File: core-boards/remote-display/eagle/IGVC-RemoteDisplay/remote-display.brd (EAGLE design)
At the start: 92 x 52.5 mm, 32 parts, among them IC1 ATMEGA8, J1 B2PS-VH(LF)(SN), SW1 SPST_TACT-EVQQ2, T1 R-78E5.0-1.0, U1 ST7920, U2 MIC550X, X1 16MHz

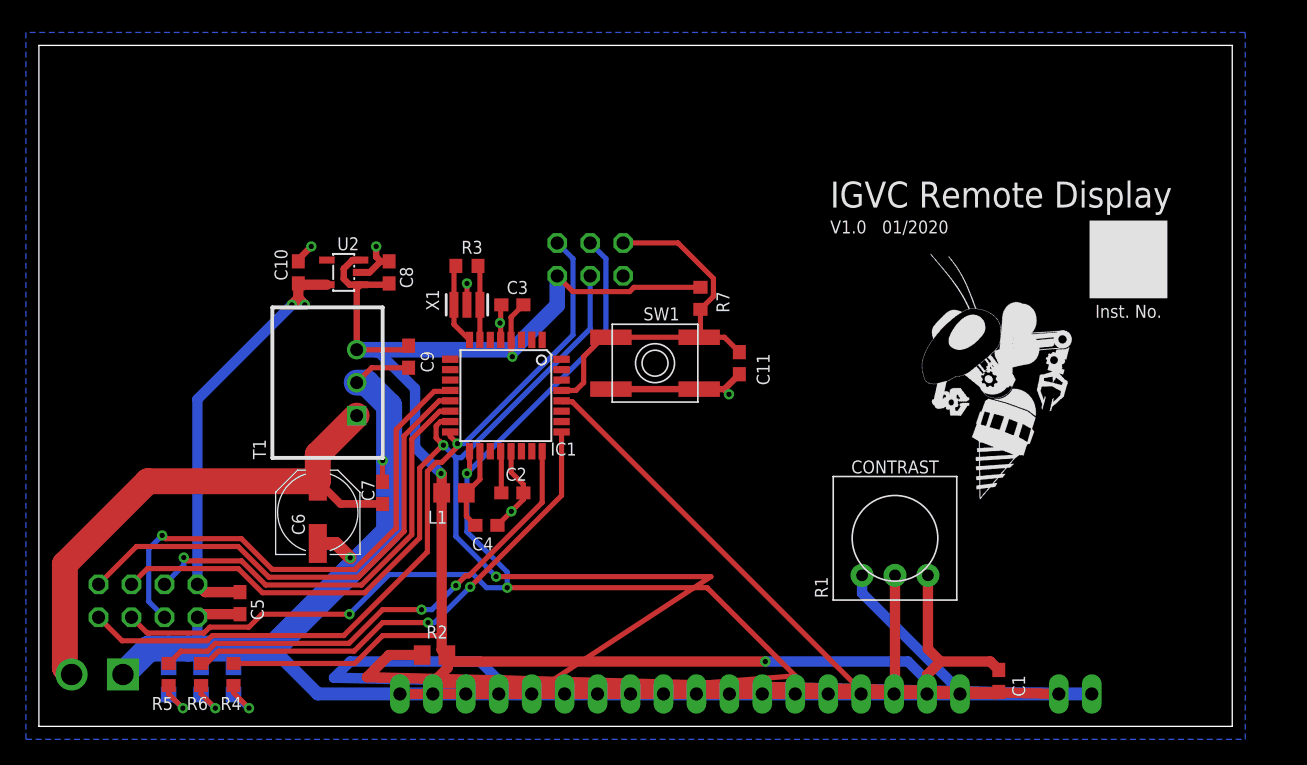
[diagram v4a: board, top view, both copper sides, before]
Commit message: Reroute Remote Display Panel
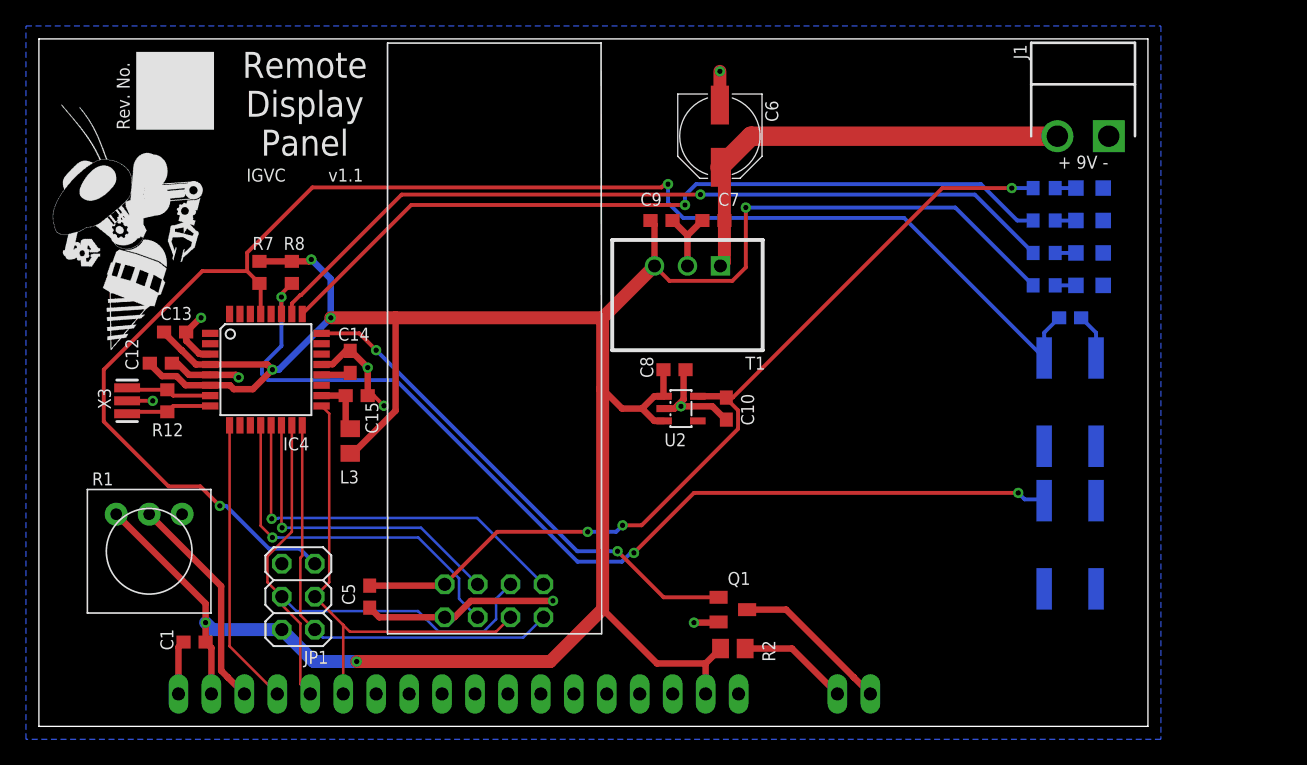
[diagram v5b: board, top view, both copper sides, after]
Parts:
- removed C2, C3, C4: 0.1uF, resistor:C0603
- removed IC1: ATMEGA8, atmel:TQFP32-08
- removed L1: 10uH, IGVC-Remote:0805
- removed U$1: ROBOBUZZ1.0X, RoboJackets-Aesthetics:ROBOBUZZ_1.0X
- removed X1: 16MHz, IGVC-Remote:RESONATOR
- added 3V3_ON: GREEN, led:CHIP-LED0805
- added C12, C13, C14, C15: 0.1uF, resistor:C0603
- added IC4: MEGA8-AI, atmel:TQFP32-08
- added L3: 10uH, IGVC-Remote:0805
- added Q1: (no value), adafruit:SOT23
- added R12: 1M, resistor:R0603
- added R8: 10K, resistor:R0603
- added SW2: SPST_TACT-EVQQ2, adafruit:EVQ-Q2
- added U$2: ROBOBUZZ1.0X, RoboJackets-Aesthetics:ROBOBUZZ_1.0X
- added X3: 16MHz, IGVC-Remote:RESONATOR
- R3: value 1M -> 220R
- moved J1 86.6 mm to (80.5, 45.5), flipped to the top, turned to 180 degrees
- moved D1 79.4 mm to (81.0, 39.0), turned to 90 degrees
- moved R5 76.0 mm to (77.5, 39.0), flipped to the bottom, turned to 180 degrees
- moved D2 76.0 mm to (81.0, 36.5), turned to 90 degrees
- moved ON 72.7 mm to (81.0, 34.0), turned to 90 degrees
- moved R6 72.7 mm to (77.5, 36.5), flipped to the bottom, turned to 180 degrees
- moved R4 69.3 mm to (77.5, 34.0), flipped to the bottom, turned to 180 degrees
- moved C1 62.1 mm to (12.0, 6.50), turned to 180 degrees
- moved R1 57.5 mm to (8.50, 13.5), turned to 180 degrees
- moved R3 44.9 mm to (77.5, 41.5), flipped to the bottom
- moved C6 42.4 mm to (52.5, 45.5), turned to 270 degrees
- moved C10 34.6 mm to (53.0, 24.5), turned to 270 degrees
- moved JP1 34.4 mm to (20.0, 10.0), flipped to the top, turned to 90 degrees
- moved R7 34.1 mm to (17.0, 35.0)
- moved C7 33.0 mm to (52.0, 39.0), turned to 180 degrees
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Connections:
- net N$3 renamed LCD_BL
- removed net STAT1: IC1.24, R5.1
- removed net STAT2: IC1.25, R6.1
- new net BL_DRAIN: Q1.3, U1.20
- new net BL_GATE: IC4.24, Q1.1
- new net BL_SW: IC4.27, R8.1, SW2.B
- new net DEBUG1: IC4.25, R5.1
- new net DEBUG2: IC4.26, R6.1
- new net PWR_LED1: 3V3_ON.A, R3.2
- net !RESET: now also IC4.29; no longer IC1.29, SW1.B'
- net +3V3: now also R3.1
- net +5V: now also C12.1, C13.1, IC4.4, IC4.6, L3.2, R8.2; no longer C3.1, IC1.4, L1.2
- net AREF: now also C14.1, IC4.20; no longer C2.1, IC1.20
- net AVCC: now also C15.1, IC4.18, L3.1; no longer C4.1, IC1.18, L1.1
- net GDO0: now also IC4.12; no longer IC1.12
- net GDO2: now also IC4.13; no longer IC1.13
- net GND: now also 3V3_ON.C, C12.2, C13.2, C14.2, C15.2, IC4.21, IC4.3, IC4.5, Q1.2, SW2.A, SW2.A', X3.2; no longer C2.2, C3.2, C4.2, IC1.21, IC1.5, U1.20, X1.2
- net LCD_CS: now also IC4.9; no longer IC1.28
- net MISO: now also IC4.16; no longer IC1.16
- net MOSI: now also IC4.15; no longer IC1.15
- net RF_CS: now also IC4.14; no longer IC1.14
- net SCK: now also IC4.17; no longer IC1.17
- net XTAL1: now also IC4.7, R12.2, X3.1; no longer IC1.7, R3.1, X1.3
- net XTAL2: now also IC4.8, R12.1, X3.3; no longer IC1.8, R3.2, X1.1
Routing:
- net GND: track 353.4 -> 61.6 mm, vias 8 -> 9
- net !RESET: track 30.1 -> 117.8 mm, vias 0 -> 2
- net BL_SW: track 0.00 -> 78.0 mm, vias 0 -> 3
- net SCK: track 109.2 -> 37.4 mm, vias 3 -> 0
- net DEBUG2: track 0.00 -> 63.3 mm, vias 0 -> 1
- net DEBUG1: track 0.00 -> 62.1 mm, vias 0 -> 1
- net MOSI: track 99.6 -> 44.0 mm, vias 2 -> 0
- net LCD_BL: track 58.3 -> 8.56 mm
- net BL_GATE: track 0.00 -> 39.0 mm, vias 0 -> 2
- net LCD_CS: track 60.3 -> 22.2 mm
- net STAT2: track 38.1 -> 0.00 mm, vias 2 -> 0
- net STAT1: track 37.9 -> 0.00 mm, vias 2 -> 0
- net +3V3: track 33.9 -> 68.9 mm, vias 2 -> 3
- net CONTRAST: track 42.2 -> 16.9 mm
- net MISO: track 59.6 -> 34.8 mm, vias 1 -> 0
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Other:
- board size 92 x 52.5 mm -> 85.5 x 53 mm
- board text added: "+ 9V -"
- board text added: "3.3V"
- board text added: "5V"
- board text added: "D1"
- board text added: "D2"
- board text added: "IGVC"
- board text added: "Remote Display Panel"
- board text added: "Rev. No."
- board text added: "v1.1"
- board text removed: "- 9V +"
- board text removed: "01/2020"
- board text removed: "CONTRAST"
- board text removed: "IGVC Remote Display"
- board text removed: "Inst. No."
- board text removed: "V1.0"

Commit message: Extraneous changes to remote display
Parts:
- added C2: 10uF, resistor:C0805
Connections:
- net +5V: now also C2.1
- net GND: now also C2.2
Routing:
- net GND: track 61.6 -> 63.5 mm, vias 9 -> 10
- net +5V: track 211.8 -> 212.8 mm
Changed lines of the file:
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@@
 <attribute name="VALUE" x="50.325" y="10.905" size="1.27" layer="27" rot="R270"/>
+</element>
+<element name="C2" library="resistor" library_urn="urn:adsk.eagle:library:348" package="C0805" package3d_urn="urn:adsk.eagle:package:23617/2" value="10uF" x="25" y="33.5" smashed="yes" rot="R90">
+<attribute name="NAME" x="23.365" y="32.865" size="1" layer="25" rot="R90"/>
+<attribute name="VALUE" x="26.905" y="32.865" size="1.27" layer="27" rot="R90"/>
 </element>
 </elements>
@@
 <wire x1="52.5" y1="47.9" x2="52.5" y2="50.5" width="1" layer="1"/>
 <via x="52.5" y="50.5" extent="1-16" drill="0.4"/>
+<contactref element="C2" pad="2"/>
+<wire x1="25" y1="34.45" x2="25" y2="35" width="0.5" layer="1"/>
+<wire x1="25" y1="35" x2="26" y2="36" width="0.5" layer="1"/>
+<via x="26" y="36" extent="1-16" drill="0.4"/>
 </signal>
 <signal name="!RESET">
@@
 <wire x1="43.46" y1="31.5" x2="27.5" y2="31.5" width="1" layer="1"/>
 <via x="22.5" y="31.5" extent="1-16" drill="0.4"/>
-<wire x1="27.5" y1="31.5" x2="22.5" y2="31.5" width="1" layer="1"/>
+<wire x1="27.5" y1="31.5" x2="25" y2="31.5" width="1" layer="1"/>
+<wire x1="25" y1="31.5" x2="22.5" y2="31.5" width="1" layer="1"/>
 <wire x1="22.5" y1="31.5" x2="22.5" y2="34.5" width="0.5" layer="16"/>
 <wire x1="22.5" y1="34.5" x2="21" y2="36" width="0.5" layer="16"/>
@@
 <wire x1="54.5" y1="35.3863125" x2="54.5" y2="40" width="0.3" layer="1"/>
 <wire x1="53.4596875" y1="34.346" x2="54.5" y2="35.3863125" width="0.3" layer="1"/>
+<contactref element="C2" pad="1"/>
+<wire x1="25" y1="32.55" x2="25" y2="31.5" width="0.5" layer="1"/>
 </signal>
 <signal name="AREF">

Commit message: Internal review remote display
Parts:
- moved 3V3_ON 7.50 mm to (81.0, 34.0)
- moved C11 7.50 mm to (79.5, 24.0)
- moved D1 7.50 mm to (81.0, 31.5)
- moved D2 7.50 mm to (81.0, 29.0)
- moved J1 7.50 mm to (80.5, 38.0)
- moved ON 7.50 mm to (81.0, 26.5)
- moved R3 7.50 mm to (77.5, 34.0)
- moved R4 7.50 mm to (77.5, 26.5)
- moved R5 7.50 mm to (77.5, 31.5)
- moved R6 7.50 mm to (77.5, 29.0)
- moved SW1 7.50 mm to (79.5, 17.5)
- moved SW2 7.50 mm to (79.5, 6.50)
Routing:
- net BL_SW: track 78.0 -> 85.5 mm
- net +5V: track 212.8 -> 215.9 mm
- net !RESET: track 117.8 -> 120.9 mm
- net DEBUG2: track 63.3 -> 66.4 mm
- net DEBUG1: track 62.1 -> 65.2 mm
- net +3V3: track 68.9 -> 65.9 mm
- net VIN: track 34.9 -> 36.0 mm
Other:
- outline, holes or cut-outs redrawn

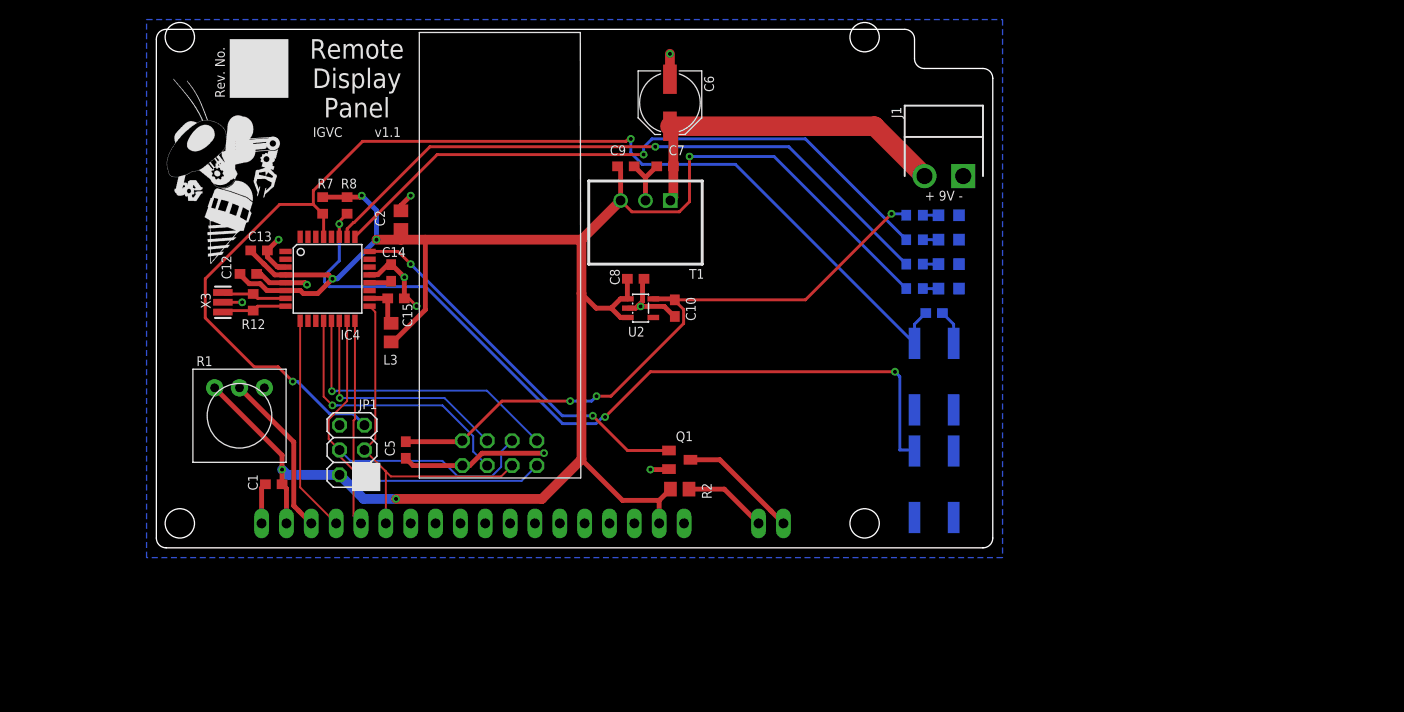
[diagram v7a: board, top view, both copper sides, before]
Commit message: Remote display design review changes, part 1
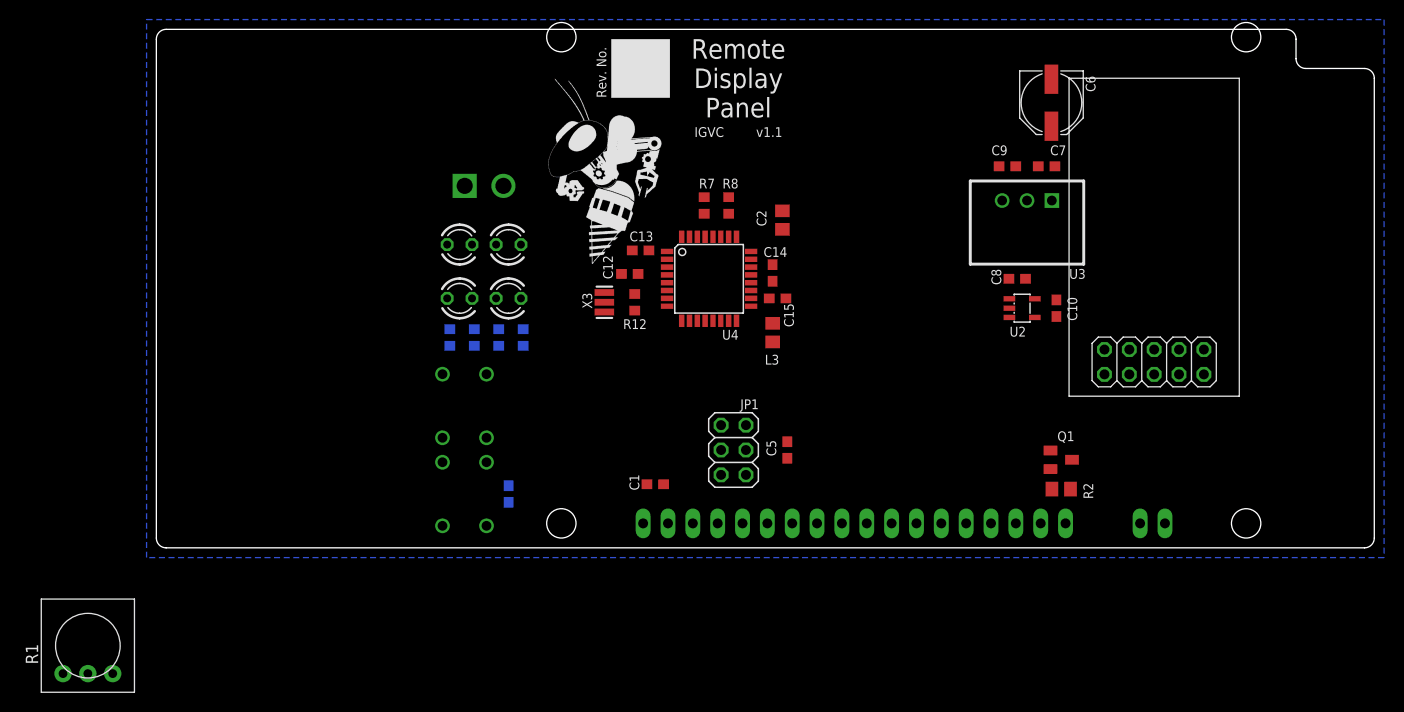
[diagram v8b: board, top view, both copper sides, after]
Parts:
- removed 3V3_ON, ON: GREEN, led:CHIP-LED0805
- removed IC4: MEGA8-AI, atmel:TQFP32-08
- removed SW1, SW2: SPST_TACT-EVQQ2, adafruit:EVQ-Q2
- removed T1: R-78E5.0-1.0, MotorBoardDev:R-78E
- removed X2: (no value), IGVC-Connector:NRF24L01+PA+LNA
- added D3, D4: GREEN, led:LED3MM
- added SW3, SW4: TL1105_A-H, IGVC-Switches:TL1105_A-H
- added U3: R-78E5.0-1.0, MotorBoardDev:R-78E
- added U4: MEGA8-AI, atmel:TQFP32-08
- added U5: (no value), IGVC-Connector:TI-CC1101
- D1: value RED -> YELLOW; device led:CHIP-LED0805 -> led:LED3MM
- D2: device led:CHIP-LED0805 -> led:LED3MM
- moved D2 50.1 mm to (31.0, 25.5), flipped to the top, turned to 0 degrees
- moved R4 47.8 mm to (30.0, 21.5), turned to 90 degrees
- moved C11 47.3 mm to (36.0, 5.50), turned to 90 degrees
- moved J1 47.0 mm to (33.5, 37.0), flipped to the bottom
- moved R6 45.6 mm to (32.5, 21.5), turned to 90 degrees
- moved D1 45.4 mm to (36.0, 25.5), flipped to the top, turned to 0 degrees
- moved R5 43.7 mm to (35.0, 21.5), turned to 90 degrees
- moved R3 41.9 mm to (37.5, 21.5), turned to 90 degrees
- moved C1 39.0 mm to (51.0, 6.50)
- moved C10 39.0 mm to (92.0, 24.5)
- moved C12 39.0 mm to (48.4, 28.0)
- moved C13 39.0 mm to (49.5, 30.4)
- moved C14 39.0 mm to (63.0, 28.1)
- moved C15 39.0 mm to (63.5, 25.5)
- moved C2 39.0 mm to (64.0, 33.5)
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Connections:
- removed net RF_CS: IC4.14, X2.CSN
- removed net VIN: C6.+, C7.1, J1.2, T1.1
- new net !RF_CS!: U4.14, U5.CSN
- new net +9V: C6.+, C7.1, J1.2, U3.1
- net !RESET: now also SW3.4, U4.29; no longer IC4.29, SW1.B
- net +3V3: now also U5.VCC1, U5.VCC2; no longer X2.VCC
- net +5V: now also U3.3, U4.4, U4.6; no longer IC4.4, IC4.6, T1.3
- net AREF: now also U4.20; no longer IC4.20
- net AVCC: now also U4.18; no longer IC4.18
- net BL_GATE: now also U4.24; no longer IC4.24
- net BL_SW: now also SW4.4, U4.27; no longer IC4.27, SW2.B
- net DEBUG1: now also U4.25; no longer IC4.25
- net DEBUG2: now also U4.26; no longer IC4.26
- net GDO0: now also U4.12, U5.GD0; no longer IC4.12, X2.CE
- net GDO2: now also U4.13, U5.GD2; no longer IC4.13, X2.IRQ
- net GND: now also D1.K, D2.K, D3.K, D4.K, SW3.1, SW3.2, SW4.1, SW4.2, U3.2, U4.21, U4.3, U4.5, U5.GND1, U5.GND2; no longer 3V3_ON.C, D1.C, D2.C, IC4.21, IC4.3, IC4.5, ON.C, SW1.A, SW1.A', SW2.A, SW2.A', T1.2, X2.GND
- net LCD_CS: now also U4.9; no longer IC4.9
- net MISO: now also U4.16, U5.SO; no longer IC4.16, X2.MISO
- net MOSI: now also U4.15, U5.SI; no longer IC4.15, X2.MOSI
- net PWR_LED: now also D3.A; no longer ON.A
- net PWR_LED1: now also D4.A; no longer 3V3_ON.A
- net SCK: now also U4.17, U5.SCK; no longer IC4.17, X2.SCK
- net XTAL1: now also U4.7; no longer IC4.7
- net XTAL2: now also U4.8; no longer IC4.8
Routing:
- net +5V: track 215.9 -> 0.00 mm, vias 6 -> 0
- net !RESET: track 120.9 -> 0.00 mm, vias 2 -> 0
- net BL_SW: track 85.5 -> 0.00 mm, vias 3 -> 0
- net DEBUG2: track 66.4 -> 0.00 mm, vias 1 -> 0
- net +3V3: track 65.9 -> 0.00 mm, vias 3 -> 0
- net DEBUG1: track 65.2 -> 0.00 mm, vias 1 -> 0
- net GND: track 63.5 -> 0.00 mm, vias 10 -> 0
- net MOSI: track 44.0 -> 0.00 mm
- net BL_GATE: track 39.0 -> 0.00 mm, vias 2 -> 0
- net SCK: track 37.4 -> 0.00 mm
- net VIN: track 36.0 -> 0.00 mm
- net MISO: track 34.8 -> 0.00 mm
- net GDO2: track 30.3 -> 0.00 mm, vias 1 -> 0
- net GDO0: track 28.3 -> 0.00 mm, vias 1 -> 0
- net RF_CS: track 24.8 -> 0.00 mm, vias 1 -> 0
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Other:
- board size 85.5 x 53 mm -> 124.5 x 53 mm
- board text removed: "3.3V"
